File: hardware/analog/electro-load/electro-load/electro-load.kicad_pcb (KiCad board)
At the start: 2 copper layers, 180 x 119 mm, 140 parts, among them J1 AVR-ISP-10, J2 Conn_WallSocket_Earth, J3 INPUT, K1 SANYOU_SRD_Form_C, M1 Noctua NF-A14 5V, Q1 2N2222A, Q2 2N2222A, Q3 IPP037N06L3, Q4 IPP037N06L3, Q5 2N2222, Q6 IPP037N06L3, Q7 IPP037N06L3, SW2 ROT_ENC, U1 ATmega328P-AU, U10 ADS1115IDGS, U11 ADS1115IDGS, U12 LMV321, U13 LMV321, U14 LM7805_TO220, U2 MCP4725A0T-E_CH, U3 LMV324, U4 RC1602A, U5 LMV324, U6 LMV324, U7 LMV324, U8 REF5040ID, U9 LMV321

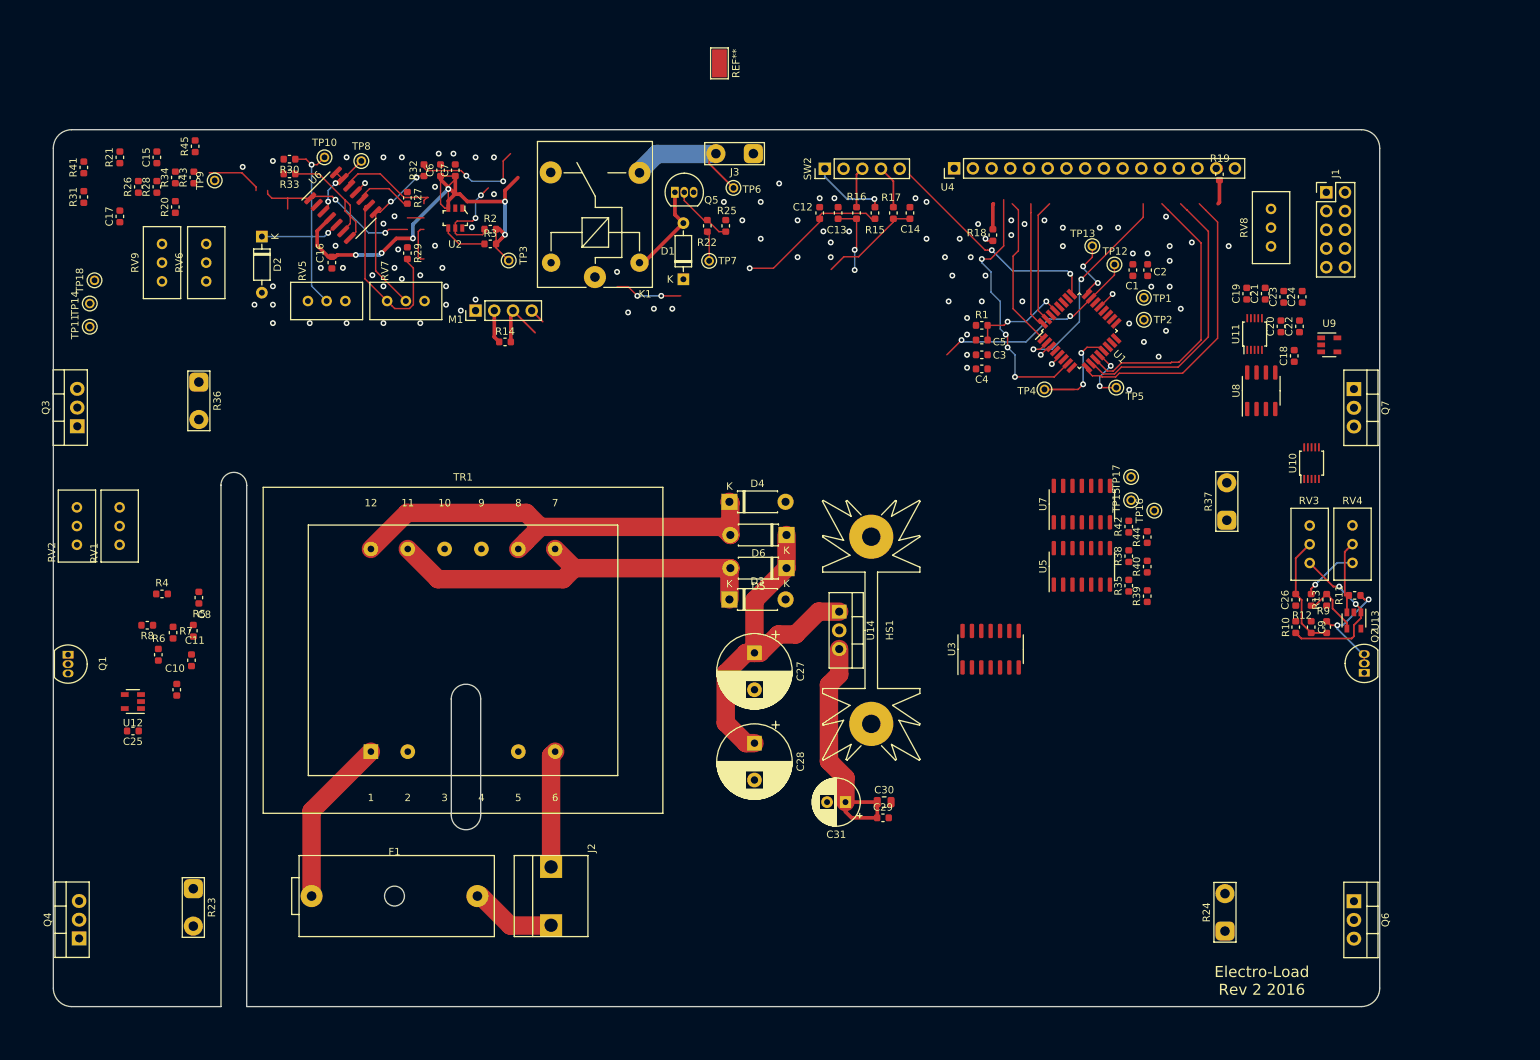
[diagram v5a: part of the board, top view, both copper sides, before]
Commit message: Changed pin connections to/from lmv324 in order to avoid bird nesting. Widened traces for 5V and LOAD_CURRENT. Added four power resistors to the fab layer. Arranged left side analogs
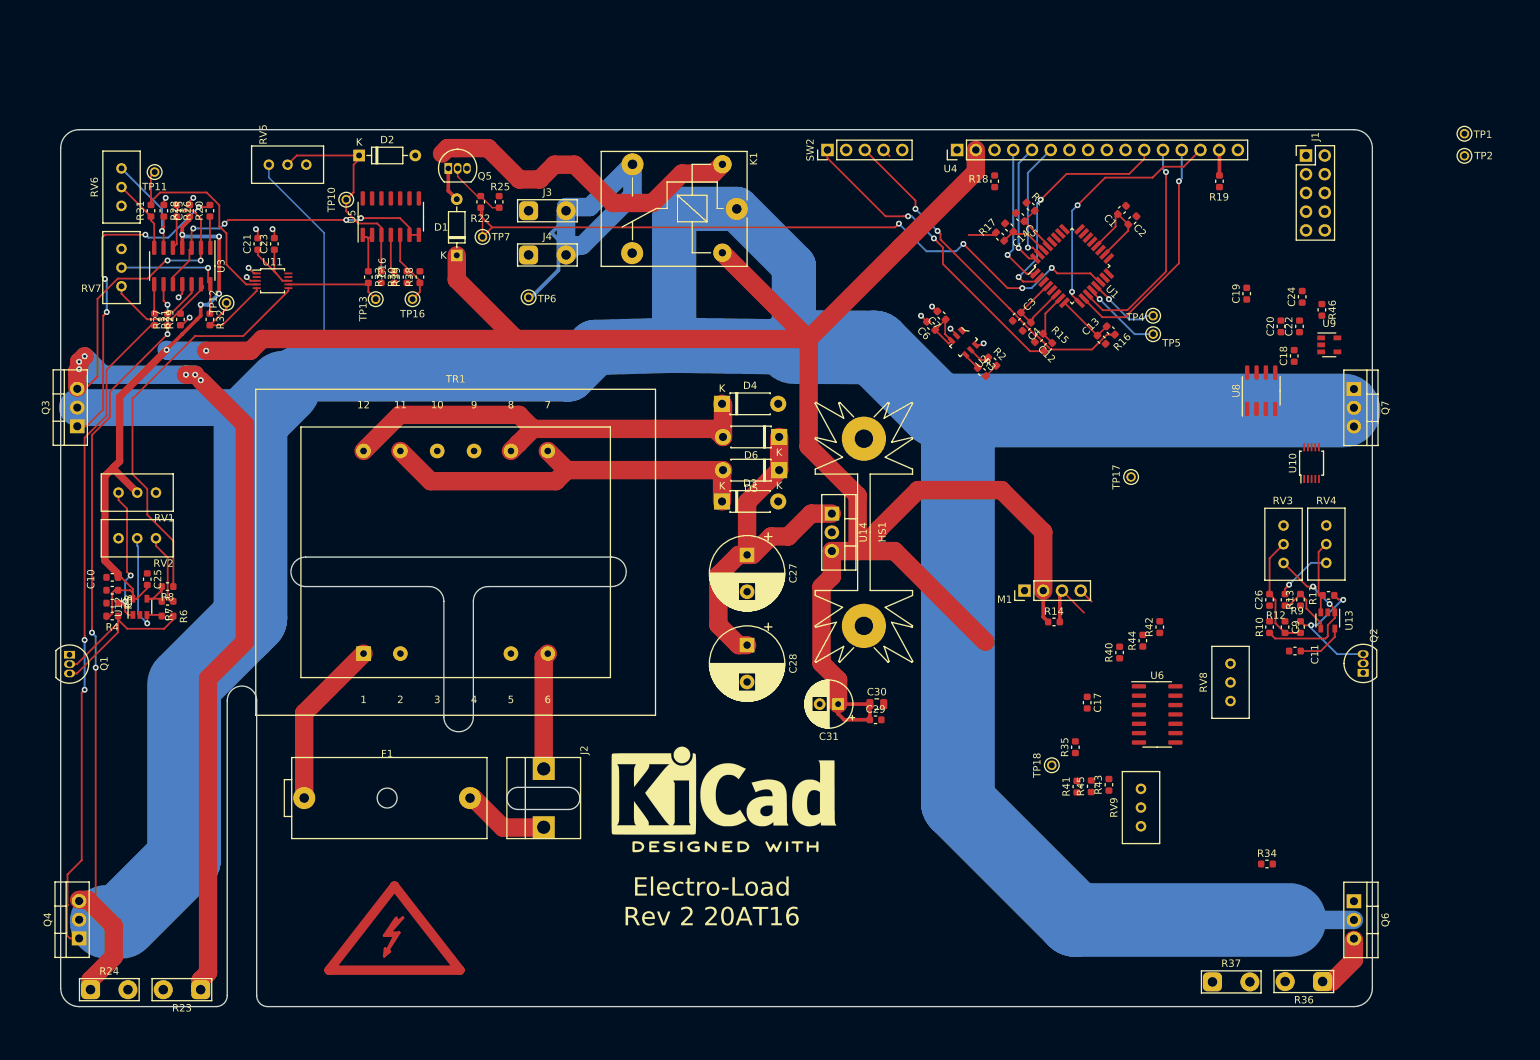
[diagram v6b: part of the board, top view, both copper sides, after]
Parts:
- removed the REF** at (151.9, 20.0)
- removed TP14, TP15, TP3, TP8, TP9: TestPoint, athir:testpoint_probe
- removed the U3 at (188.7, 99.5)
- removed U7: LMV324, Package_SO:SOIC-14_3.9x8.7mm_P1.27mm
- added J4: INPUT, TestPoint:TestPoint_2Pads_Pitch5.08mm_Drill1.3mm, F.Cu at (126.0, 46.0)
- added R46: 1k, Resistor_SMD:R_0603_1608Metric, F.Cu at (233.7, 53.5)
- added REF**: KiCad-Logo2_12mm_SilkScreen, Symbol:KiCad-Logo2_12mm_SilkScreen, F.Cu at (152.5, 118.7)
- added REF**: Symbol_Highvoltage_Type2_CopperTop_Small, Symbol:Symbol_Highvoltage_Type2_CopperTop_Small, F.Cu at (107.8, 139.2)
- added U6: LMV324, Package_SO:SOIC-14_3.9x8.7mm_P1.27mm, F.Cu at (211.3, 108.3)
- moved R34 175.0 mm to (226.2, 128.7), turned to 0 degrees
- moved R36 172.8 mm to (233.8, 144.6), turned to 180 degrees
- moved R41 158.8 mm to (200.4, 118.2)
- moved R24 154.2 mm to (66.5, 145.7), turned to 0 degrees
- moved RV9 152.0 mm to (209.1, 118.5)
- moved C11 149.8 mm to (230.0, 99.8), turned to 180 degrees
- moved R45 149.4 mm to (202.3, 118.1)
- moved R43 149.0 mm to (204.8, 117.9)
- moved C17 146.9 mm to (201.8, 106.8), turned to 270 degrees
- moved TP18 145.6 mm to (197.0, 115.2)
- moved C23 137.2 mm to (91.5, 44.5)
- moved C21 136.9 mm to (89.2, 44.5)
- moved U11 133.5 mm to (91.2, 49.5), turned to 0 degrees
- moved TP12 120.6 mm to (85.0, 52.5), turned to 0 degrees
- moved R39 109.4 mm to (109.5, 49.0)
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- renumbered U6 to U3
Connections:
- Q4 pad 1: Net-(Q4-Pad1) -> /Current Measurements/LOAD_CURRENT
- Q4 pad 3: Net-(Q4-Pad3) -> /Current Measurements/LOAD_CURRENT
- R21 pad 2: Net-(Q4-Pad1) -> /Current Measurements/LOAD_CURRENT
- R24 pad 1: Net-(Q4-Pad3) -> /Current Measurements/LOAD_CURRENT
- R27 pad 1: Net-(Q4-Pad3) -> /Current Measurements/LOAD_CURRENT
- U10 pad 4: /Current Measurements/V_MEAS -> /Current Measurements/CUR_MEAS_2
- U10 pad 5: /Temperature Control/TEMP_0 -> /Current Measurements/CUR_MEAS_3
- U10 pad 6: /Temperature Control/TEMP_1 -> /Temperature Control/TEMP_0
- U10 pad 7: GND -> Net-(R46-Pad1)
- U11 pad 6: /Current Measurements/CUR_MEAS_2 -> /Temperature Control/TEMP_1
- U11 pad 7: /Current Measurements/CUR_MEAS_3 -> /Current Measurements/V_MEAS
- U3 pad 1: Net-(R34-Pad1) -> Net-(R20-Pad1)
- U3 pad 10: Net-(R27-Pad2) -> /Current Measurements/CURRENT_SET
- U3 pad 12: Net-(R41-Pad2) -> Net-(R27-Pad2)
- U3 pad 13: Net-(R43-Pad2) -> Net-(R29-Pad2)
- U3 pad 14: Net-(R45-Pad1) -> Net-(R32-Pad1)
- U3 pad 2: Net-(Q6-Pad3) -> Net-(Q3-Pad3)
- U3 pad 5: (no net) -> Net-(R26-Pad2)
- U3 pad 6: (no net) -> Net-(R28-Pad2)
- U3 pad 7: (no net) -> Net-(R31-Pad1)
- U3 pad 8: Net-(R32-Pad1) -> Net-(R21-Pad1)
- U3 pad 9: Net-(R29-Pad2) -> /Current Measurements/LOAD_CURRENT
- U5 pad 10: /Current Measurements/CURRENT_SET -> (no net)
- U5 pad 12: Net-(R40-Pad2) -> (no net)
- U5 pad 13: Net-(R42-Pad2) -> (no net)
- U5 pad 14: Net-(R44-Pad1) -> (no net)
- U5 pad 8: Net-(R21-Pad1) -> (no net)
- U5 pad 9: Net-(Q4-Pad3) -> (no net)
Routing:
- net /Current Measurements/LOAD_CURRENT: track 0.00 -> 656.3 mm, vias 0 -> 6
- net +5V: track 126.6 -> 437.6 mm
- net Net-(Q3-Pad3): track 0.00 -> 153.8 mm, vias 0 -> 8
- net /RELAY_EN: track 4.50 -> 98.8 mm, vias 0 -> 4
- net /Temperature Control/TEMP_1: track 0.00 -> 55.4 mm
- net /ROT_A: track 56.7 -> 7.52 mm, vias 5 -> 0
- net Net-(R16-Pad1): track 5.54 -> 47.1 mm, vias 0 -> 2
- net /Current Measurements/CURRENT_SET: track 0.00 -> 41.4 mm, vias 0 -> 4
- net (no net): track 39.4 -> 0.00 mm, vias 4 -> 0
- net Net-(Q3-Pad1): track 7.63 -> 45.1 mm, vias 0 -> 4
- net Net-(D1-Pad2): track 12.9 -> 50.1 mm
- net Net-(D7-Pad1): track 34.8 -> 0.00 mm, vias 2 -> 0
- net Net-(J3-Pad2): track 16.4 -> 49.8 mm
- net Net-(R15-Pad1): track 10.2 -> 42.7 mm, vias 1 -> 2
- net Net-(Q1-Pad2): track 0.00 -> 29.9 mm
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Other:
- board size 180 x 119 mm -> 178 x 119 mm
- net class HV added: clearance 2.5, trace_width 2.5, via_dia 0.8, via_drill 0.4
- net class High Current added: clearance 0.3, trace_width 10, via_dia 0.8, via_drill 0.4
- board text added: "Electro-Load Rev 2 20AT16"
- board text removed: "Electro-Load Rev 2 2016"

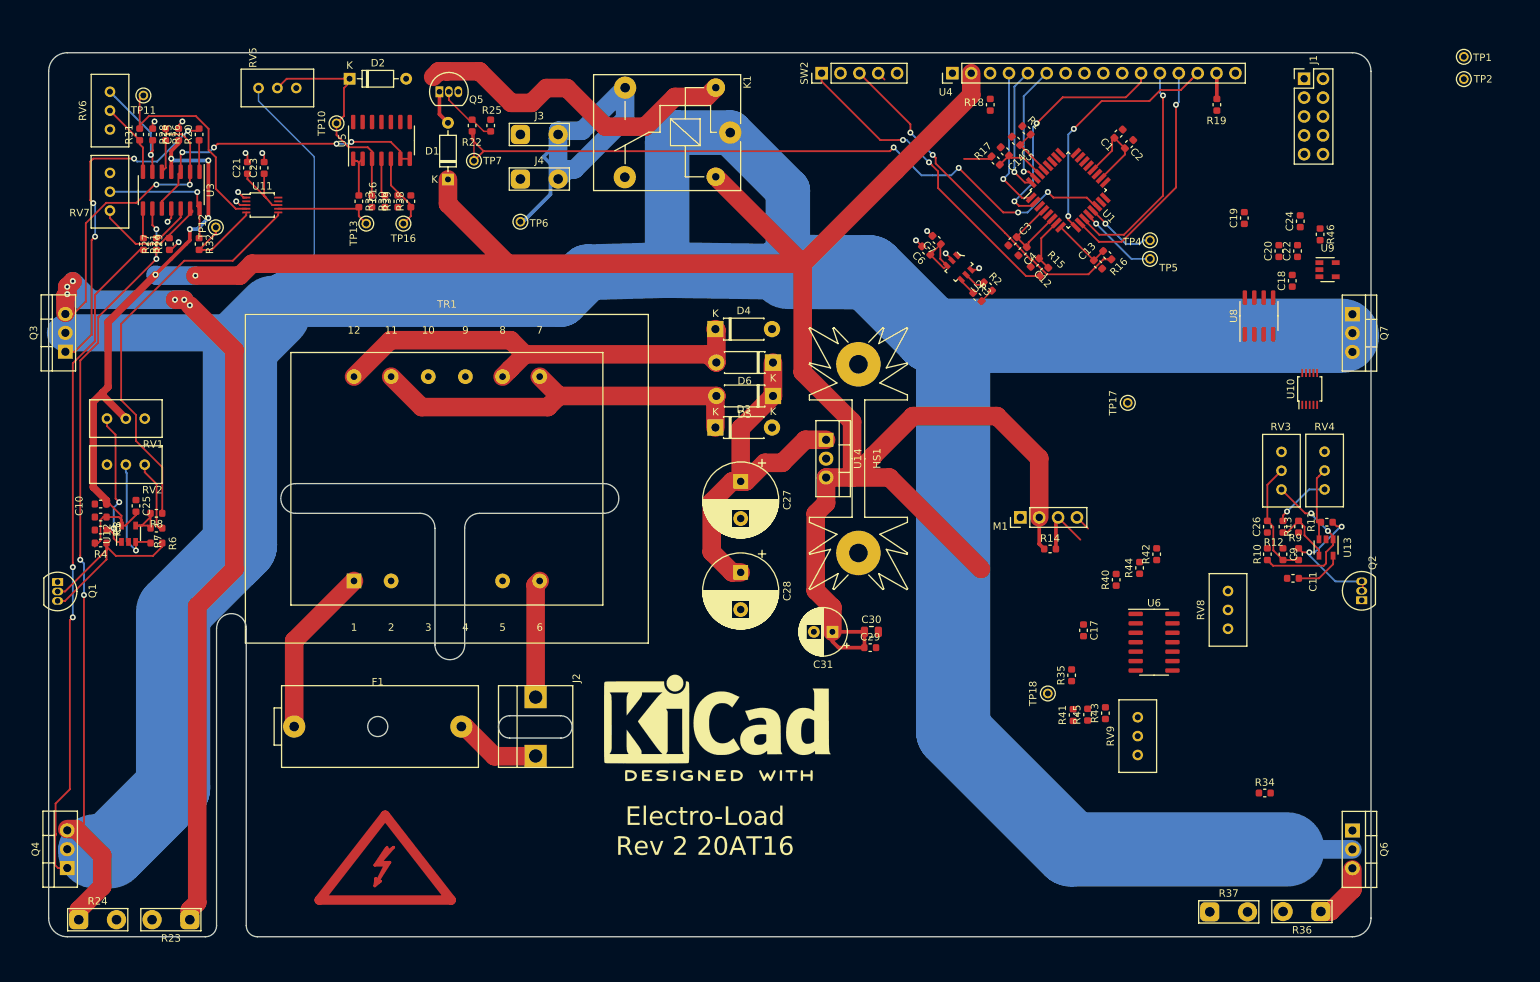
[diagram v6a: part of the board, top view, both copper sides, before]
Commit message: All traces layed out. Silkscreen and finishing touches needed.
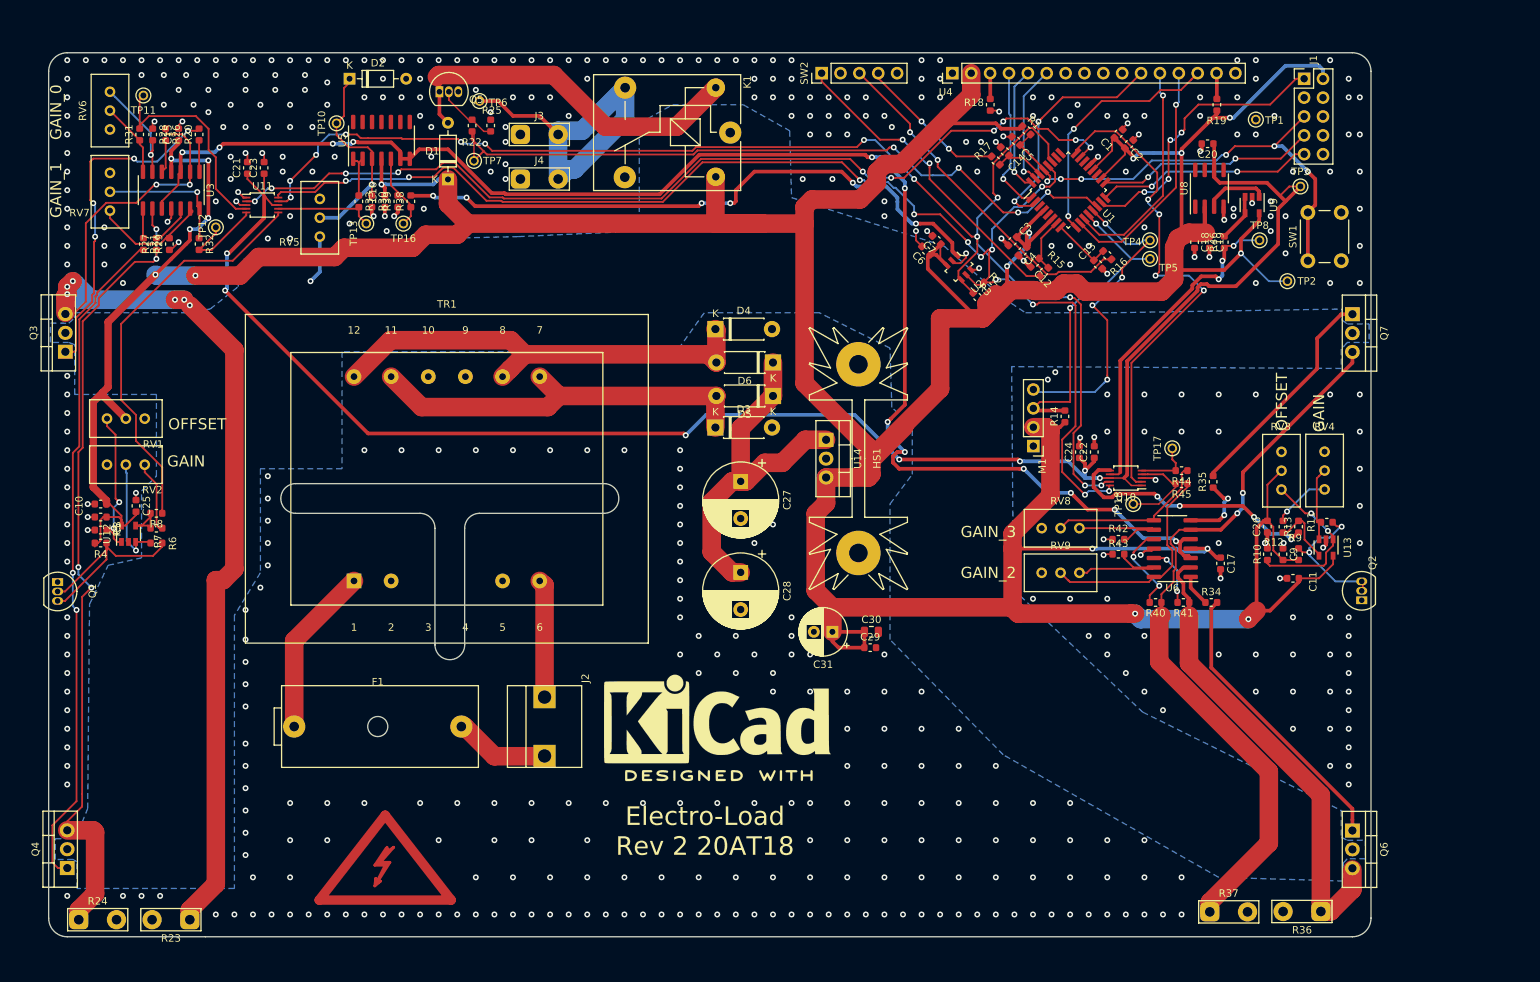
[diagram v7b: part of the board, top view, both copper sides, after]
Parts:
- added SW1: RESET, Button_Switch_THT:SW_PUSH_6mm_H4.3mm, F.Cu at (232.0, 57.0)
- added TP3: TestPoint, athir:testpoint_probe, F.Cu at (231.0, 47.0)
- added TP8: TestPoint, athir:testpoint_probe, F.Cu at (225.5, 54.2)
- moved C24 43.0 mm to (201.2, 82.8)
- moved C22 38.5 mm to (203.2, 82.8)
- moved TP2 36.1 mm to (229.2, 59.8)
- moved R45 33.6 mm to (215.0, 87.0), turned to 180 degrees
- moved R35 32.3 mm to (219.2, 86.8)
- moved TP1 29.2 mm to (225.0, 38.0)
- moved TP18 28.0 mm to (208.5, 89.8)
- moved U10 27.5 mm to (207.5, 86.2), turned to 180 degrees
- moved R34 26.6 mm to (219.0, 103.0)
- moved RV8 21.7 mm to (201.2, 93.0), turned to 0 degrees
- moved RV5 21.6 mm to (99.0, 53.8), turned to 270 degrees
- moved R43 21.5 mm to (206.5, 96.5), turned to 0 degrees
- moved R41 21.2 mm to (215.2, 103.0), turned to 180 degrees
- moved RV9 21.0 mm to (201.2, 99.0), turned to 0 degrees
- moved C17 20.5 mm to (220.2, 97.8)
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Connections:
- Q4 pad 1: /Current Measurements/LOAD_CURRENT -> Net-(Q4-Pad1)
- Q4 pad 3: /Current Measurements/LOAD_CURRENT -> Net-(Q4-Pad3)
- R21 pad 2: /Current Measurements/LOAD_CURRENT -> Net-(Q4-Pad1)
- R24 pad 1: /Current Measurements/LOAD_CURRENT -> Net-(Q4-Pad3)
- R27 pad 1: /Current Measurements/LOAD_CURRENT -> Net-(Q4-Pad3)
- R46 pad 2: GND -> Net-(R46-Pad2)
- TP1 pad 1: +5V -> GND
- U3 pad 9: /Current Measurements/LOAD_CURRENT -> Net-(Q4-Pad3)
- U9 pad 3: GND -> Net-(R46-Pad2)
- U9 pad 4: GND -> Net-(R46-Pad2)
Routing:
- net /Current Measurements/LOAD_CURRENT: track 656.3 -> 6.52 mm, vias 6 -> 1
- net +5V: track 437.6 -> 739.3 mm, vias 6 -> 17
- net +4V: track 9.68 -> 238.0 mm, vias 0 -> 7
- net /SDA: track 2.45 -> 187.7 mm, vias 0 -> 13
- net /SCL: track 3.08 -> 178.9 mm, vias 0 -> 12
- net /Current Measurements/CURRENT_SET: track 41.4 -> 203.5 mm, vias 4 -> 12
- net /ADC_0_ALERT: track 0.00 -> 127.9 mm, vias 0 -> 10
- net Net-(Q4-Pad3): track 0.00 -> 109.6 mm, vias 0 -> 4
- net Net-(Q7-Pad3): track 0.00 -> 100.7 mm, vias 0 -> 2
- net Net-(Q4-Pad1): track 0.00 -> 90.5 mm, vias 0 -> 2
- net /CUR_SET: track 0.00 -> 83.1 mm, vias 0 -> 6
- net /ADC_1_ALERT: track 0.00 -> 68.1 mm, vias 0 -> 4
- net /~RESET: track 6.68 -> 65.7 mm, vias 0 -> 6
- net Net-(Q6-Pad3): track 8.18 -> 64.8 mm
- net Net-(R46-Pad1): track 0.00 -> 44.6 mm, vias 0 -> 3
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- added copper zone on B.Cu, net /Current Measurements/LOAD_CURRENT
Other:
- outline, holes or cut-outs redrawn
- board text added: "Electro-Load Rev 2 20AT18"
- board text added: "GAIN"
- board text added: "GAIN_0"
- board text added: "GAIN_1"
- board text added: "GAIN_2"
- board text added: "GAIN_3"
- board text added: "OFFSET"
- board text removed: "Electro-Load Rev 2 20AT16"
